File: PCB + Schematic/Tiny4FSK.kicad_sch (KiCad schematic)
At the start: 83 parts, among them J1 Power Ext, J2 GPIO, J3 I2C, J4 USB, J5 USB Breakout, J6 SPI, J7 USBC, J8 SWD, J9 Counterpoise, SW1 Power Switch, SW2 RST, U1 BME280, U2 ATGM336H, U3 TPS61200DRC, U4 ECS-327TXO-2012, U5 ATSAMD21G18A-A, U6 SI4063, U7 Linear Step-Down

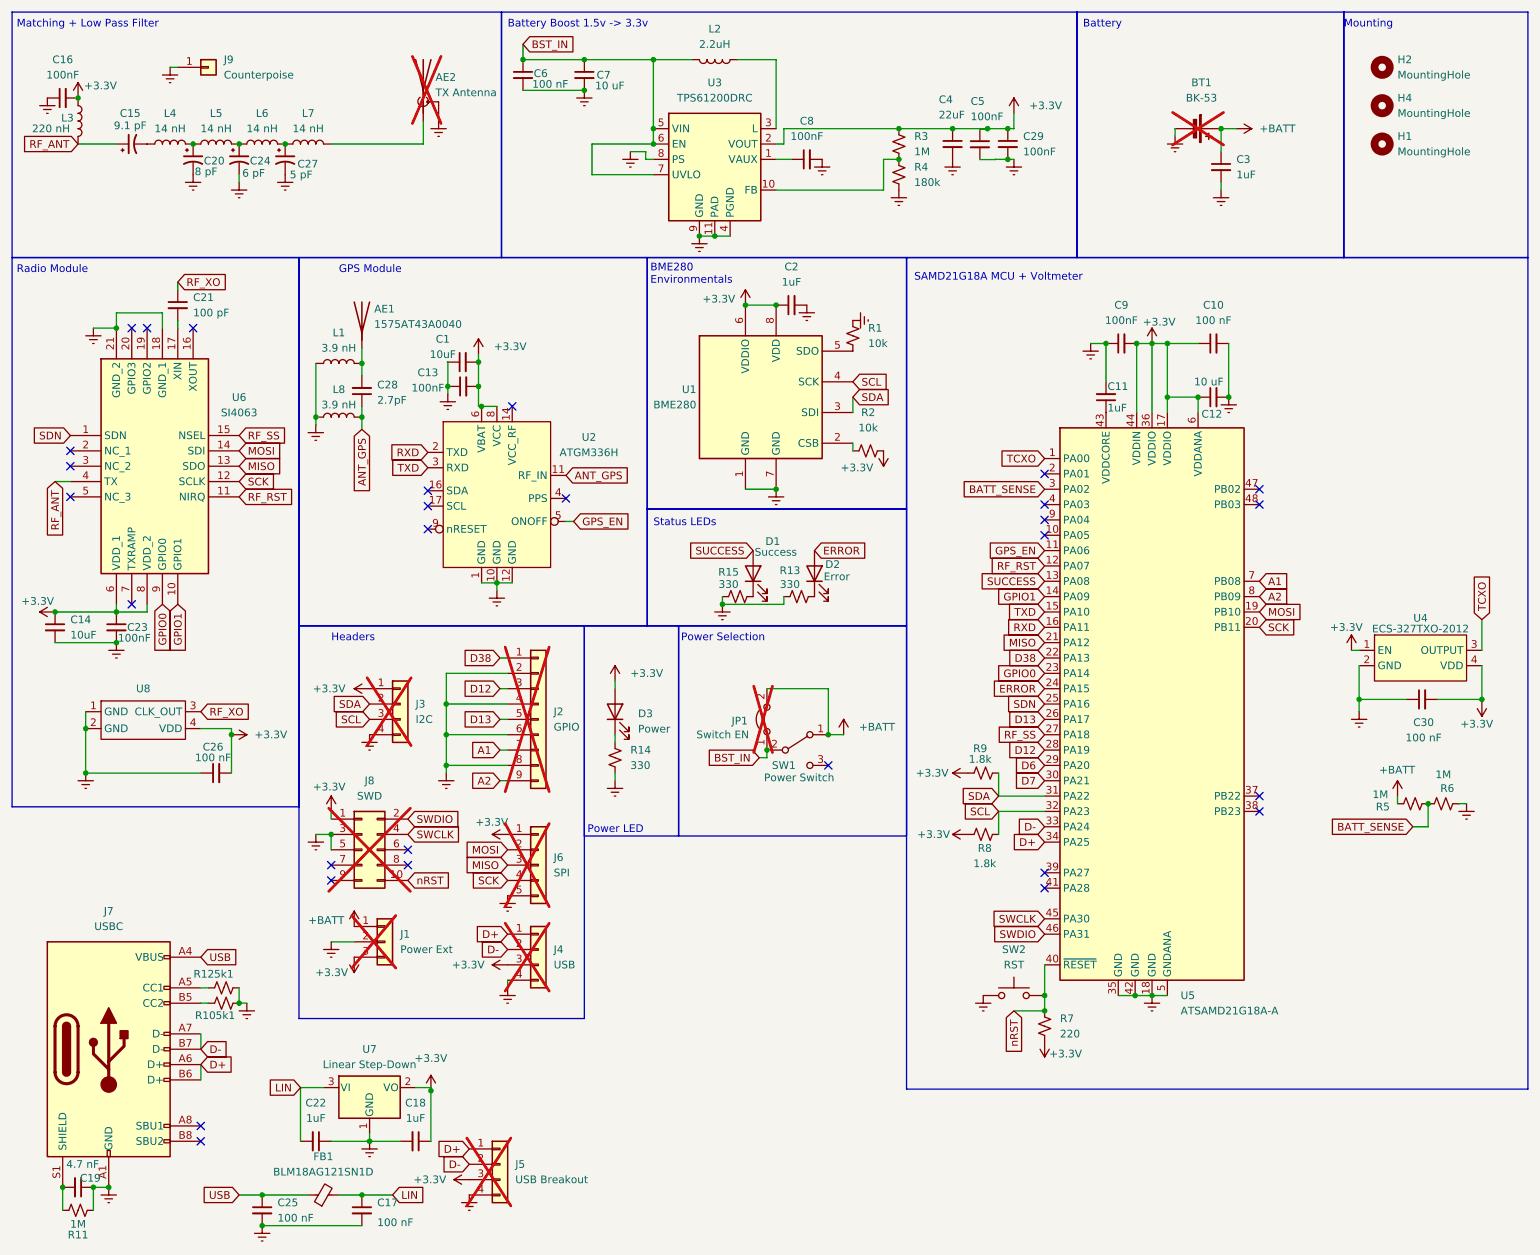
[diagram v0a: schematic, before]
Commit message: split into hierarchical sheets
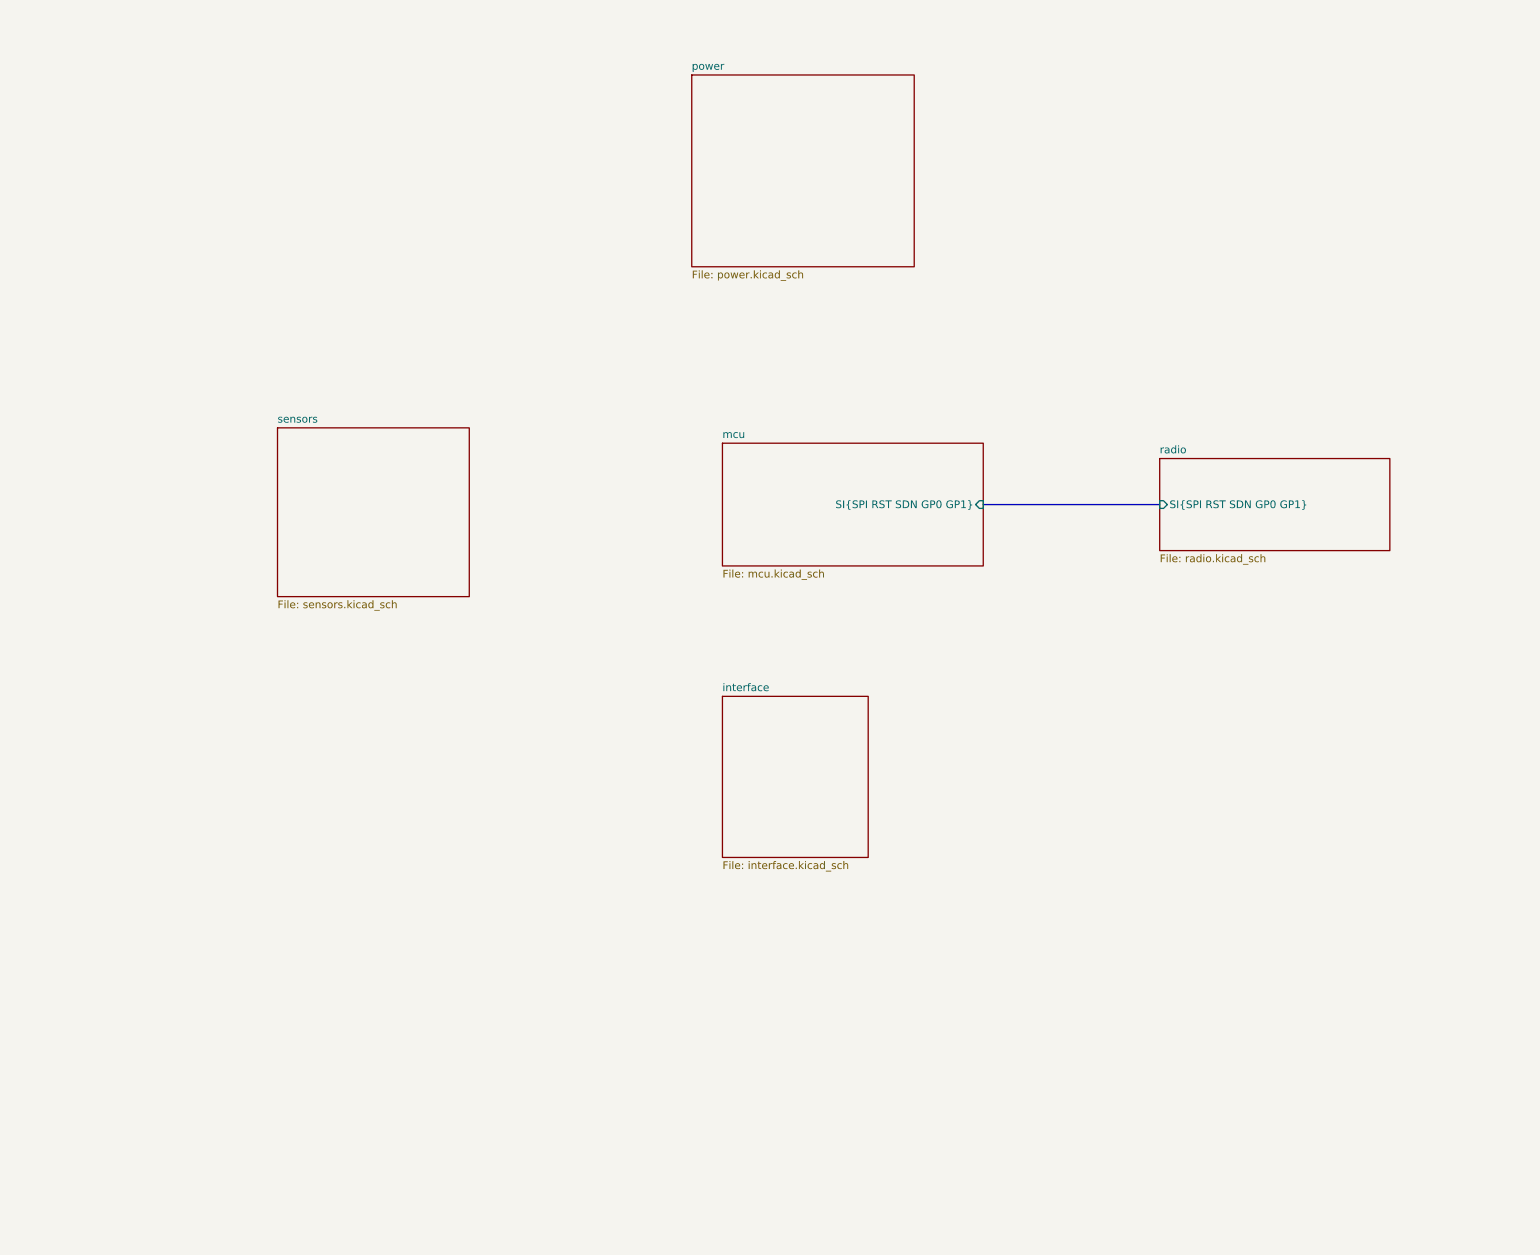
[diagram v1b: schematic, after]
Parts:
- removed AE1: 1575AT43A0040, RF_Antenna_Extended:ANT_1575AT_JOT, symbol Device:Antenna
- removed AE2: TX Antenna, Antenna:Antenna_Whip, symbol Device:Antenna_Shield
- removed BT1: BK-53, BatteryExtended:BAT_53, symbol Device:Battery_Cell
- removed C1, C14: 10uF, Capacitor_SMD:C_0402_1005Metric_Pad0.74x0.62mm_HandSolder, symbol Device:C_Small
- removed C10, C17, C25, C26, C30, C6: 100 nF, Capacitor_SMD:C_0402_1005Metric_Pad0.74x0.62mm_HandSolder, symbol Device:C_Small
- removed C11, C18, C2, C22, C3: 1uF, Capacitor_SMD:C_0402_1005Metric_Pad0.74x0.62mm_HandSolder, symbol Device:C_Small
- removed C12: 10 uF, Capacitor_SMD:C_0402_1005Metric_Pad0.74x0.62mm_HandSolder, symbol Device:C_Small
- removed C13, C16, C23, C29, C5, C8, C9: 100nF, Capacitor_SMD:C_0402_1005Metric_Pad0.74x0.62mm_HandSolder, symbol Device:C_Small
- removed C15: 9.1 pF, Capacitor_SMD:C_0402_1005Metric_Pad0.74x0.62mm_HandSolder, symbol Device:C_Polarized_Small_US
- removed C19: 4.7 nF, Capacitor_SMD:C_0402_1005Metric_Pad0.74x0.62mm_HandSolder, symbol Device:C_Small
- removed C20: 8 pF, Capacitor_SMD:C_0402_1005Metric_Pad0.74x0.62mm_HandSolder, symbol Device:C_Polarized_Small_US
- removed C21: 100 pF, Capacitor_SMD:C_0402_1005Metric_Pad0.74x0.62mm_HandSolder, symbol Device:C_Small
- removed C24: 6 pF, Capacitor_SMD:C_0402_1005Metric_Pad0.74x0.62mm_HandSolder, symbol Device:C_Polarized_Small_US
- removed C27: 5 pF, Capacitor_SMD:C_0402_1005Metric_Pad0.74x0.62mm_HandSolder, symbol Device:C_Polarized_Small_US
- removed C28: 2.7pF, Capacitor_SMD:C_0402_1005Metric_Pad0.74x0.62mm_HandSolder, symbol Device:C_Small
- removed C4: 22uF, Capacitor_SMD:C_0603_1608Metric_Pad1.08x0.95mm_HandSolder, symbol Device:C_Small
- removed C7: 10 uF, Capacitor_SMD:C_0603_1608Metric_Pad1.08x0.95mm_HandSolder, symbol Device:C_Small
- removed D1: Success, LED_SMD:LED_0805_2012Metric_Pad1.15x1.40mm_HandSolder, symbol Device:LED
- removed D2: Error, LED_SMD:LED_0805_2012Metric_Pad1.15x1.40mm_HandSolder, symbol Device:LED
- removed D3: Power, LED_SMD:LED_0805_2012Metric_Pad1.15x1.40mm_HandSolder, symbol Device:LED
- removed FB1: BLM18AG121SN1D, Resistor_SMD:R_0603_1608Metric_Pad0.98x0.95mm_HandSolder, symbol Device:FerriteBead_Small
- removed H1, H2, H4: MountingHole, MountingHole:MountingHole_2.2mm_M2, symbol Mechanical:MountingHole
- removed J1: Power Ext, Connector_PinHeader_2.54mm:PinHeader_1x03_P2.54mm_Vertical, symbol Connector_Generic:Conn_01x03
- removed J2: GPIO, Connector_PinHeader_2.54mm:PinHeader_1x09_P2.54mm_Vertical, symbol Connector_Generic:Conn_01x09
- removed J3: I2C, Connector_PinHeader_2.54mm:PinHeader_1x04_P2.54mm_Vertical, symbol Connector_Generic:Conn_01x04
- removed J4: USB, Connector_PinHeader_2.54mm:PinHeader_1x04_P2.54mm_Vertical, symbol Connector_Generic:Conn_01x04
- removed J5: USB Breakout, Connector_PinHeader_2.54mm:PinHeader_1x04_P2.54mm_Vertical, symbol Connector_Generic:Conn_01x04
- removed J6: SPI, Connector_PinHeader_2.54mm:PinHeader_1x05_P2.54mm_Vertical, symbol Connector_Generic:Conn_01x05
- removed J7: USBC, Connector_USB:USB_C_Receptacle_GCT_USB4105-xx-A_16P_TopMnt_Horizontal, symbol Connector:USB_C_Receptacle_USB2.0
- removed J8: SWD, Connector_PinHeader_1.27mm:PinHeader_2x05_P1.27mm_Vertical_SMD, symbol Connector_Generic:Conn_02x05_Odd_Even
- removed J9: Counterpoise, Connector_PinHeader_2.54mm:PinHeader_1x01_P2.54mm_Vertical, symbol Connector_Generic:Conn_01x01
- removed JP1: Switch EN, Jumper:SolderJumper-2_P1.3mm_Open_Pad1.0x1.5mm, symbol Jumper:Jumper_2_Open
- removed L1, L8: 3.9 nH, Inductor_SMD:L_0402_1005Metric_Pad0.77x0.64mm_HandSolder, symbol Device:L
- removed L2: 2.2uH, IND_CONT:LPS3015222MRB, symbol Device:L
- removed L3: 220 nH, Inductor_SMD:L_0402_1005Metric_Pad0.77x0.64mm_HandSolder, symbol Device:L
- removed L4, L5, L6, L7: 14 nH, Inductor_SMD:L_0402_1005Metric_Pad0.77x0.64mm_HandSolder, symbol Device:L
- removed R1, R2: 10k, Resistor_SMD:R_0402_1005Metric_Pad0.72x0.64mm_HandSolder, symbol Device:R_Small_US
- removed R10, R12: 5k1, Resistor_SMD:R_0402_1005Metric_Pad0.72x0.64mm_HandSolder, symbol Device:R_Small_US
- removed R11, R3, R5, R6: 1M, Resistor_SMD:R_0402_1005Metric_Pad0.72x0.64mm_HandSolder, symbol Device:R_Small_US
- removed R13, R14, R15: 330, Resistor_SMD:R_0402_1005Metric_Pad0.72x0.64mm_HandSolder, symbol Device:R_Small_US
- removed R4: 180k, Resistor_SMD:R_0402_1005Metric_Pad0.72x0.64mm_HandSolder, symbol Device:R_Small_US
- removed R7: 220, Resistor_SMD:R_0402_1005Metric_Pad0.72x0.64mm_HandSolder, symbol Device:R_Small_US
- removed R8, R9: 1.8k, Resistor_SMD:R_0402_1005Metric_Pad0.72x0.64mm_HandSolder, symbol Device:R_Small_US
- removed SW1: Power Switch, Button_Switch_SMD:SW_SPDT_PCM12, symbol Switch:SW_SPDT
- removed SW2: RST, Button_Switch_SMD:SW_Tactile_SPST_NO_Straight_CK_PTS636Sx25SMTRLFS, symbol Switch:SW_Push
- removed U1: BME280, Package_LGA:Bosch_LGA-8_2.5x2.5mm_P0.65mm_ClockwisePinNumbering, symbol Sensor:BME280
- removed U2: ATGM336H, RF_GPS_Extended:ATGM336H, symbol RF_GPS_Extended:ATGM336H
- removed U3: TPS61200DRC, Package_SON:Texas_S-PVSON-N10_ThermalVias, symbol Regulator_Switching:TPS61200DRC
- removed U4: ECS-327TXO-2012, Crystal:Crystal_SMD_3225-4Pin_3.2x2.5mm, symbol Oscillator:ATXK-H11-E-32.768KHZ-E50-T3
- removed U5: ATSAMD21G18A-A, Package_QFP:TQFP-48_7x7mm_P0.5mm, symbol MCU_Microchip_SAMD:ATSAMD21G18A-A
- removed U6: SI4063, Package_DFN_QFN:QFN-20-1EP_4x4mm_P0.5mm_EP2.5x2.5mm_ThermalVias, symbol SI4063:SI4063-C2A-GMR
- removed U7: Linear Step-Down, LDO:MCP1700, symbol Regulator_Linear:MCP1700x-330xxTT
- removed U8: (no value), Oscillator_TCXO:ECS-TXO-20CSMV4, symbol TCXO:20CSMV4
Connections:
- no-connect marks 29 -> 0
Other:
- added sheet interface (interface.kicad_sch)
- added sheet mcu (mcu.kicad_sch)
- added sheet power (power.kicad_sch)
- added sheet radio (radio.kicad_sch)
- added sheet sensors (sensors.kicad_sch)
- note removed: "BME280 Environmentals"
- note removed: "Battery"
- note removed: "Battery Boost 1.5v -> 3.3v"
- note removed: "GPS Module"
- note removed: "Headers"
- note removed: "Matching + Low Pass Filter"
- note removed: "Mounting"
- note removed: "Power LED"
- note removed: "Power Selection"
- note removed: "Radio Module"
- note removed: "SAMD21G18A MCU + Voltmeter"
- note removed: "Status LEDs"

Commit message: add power path and interface busses
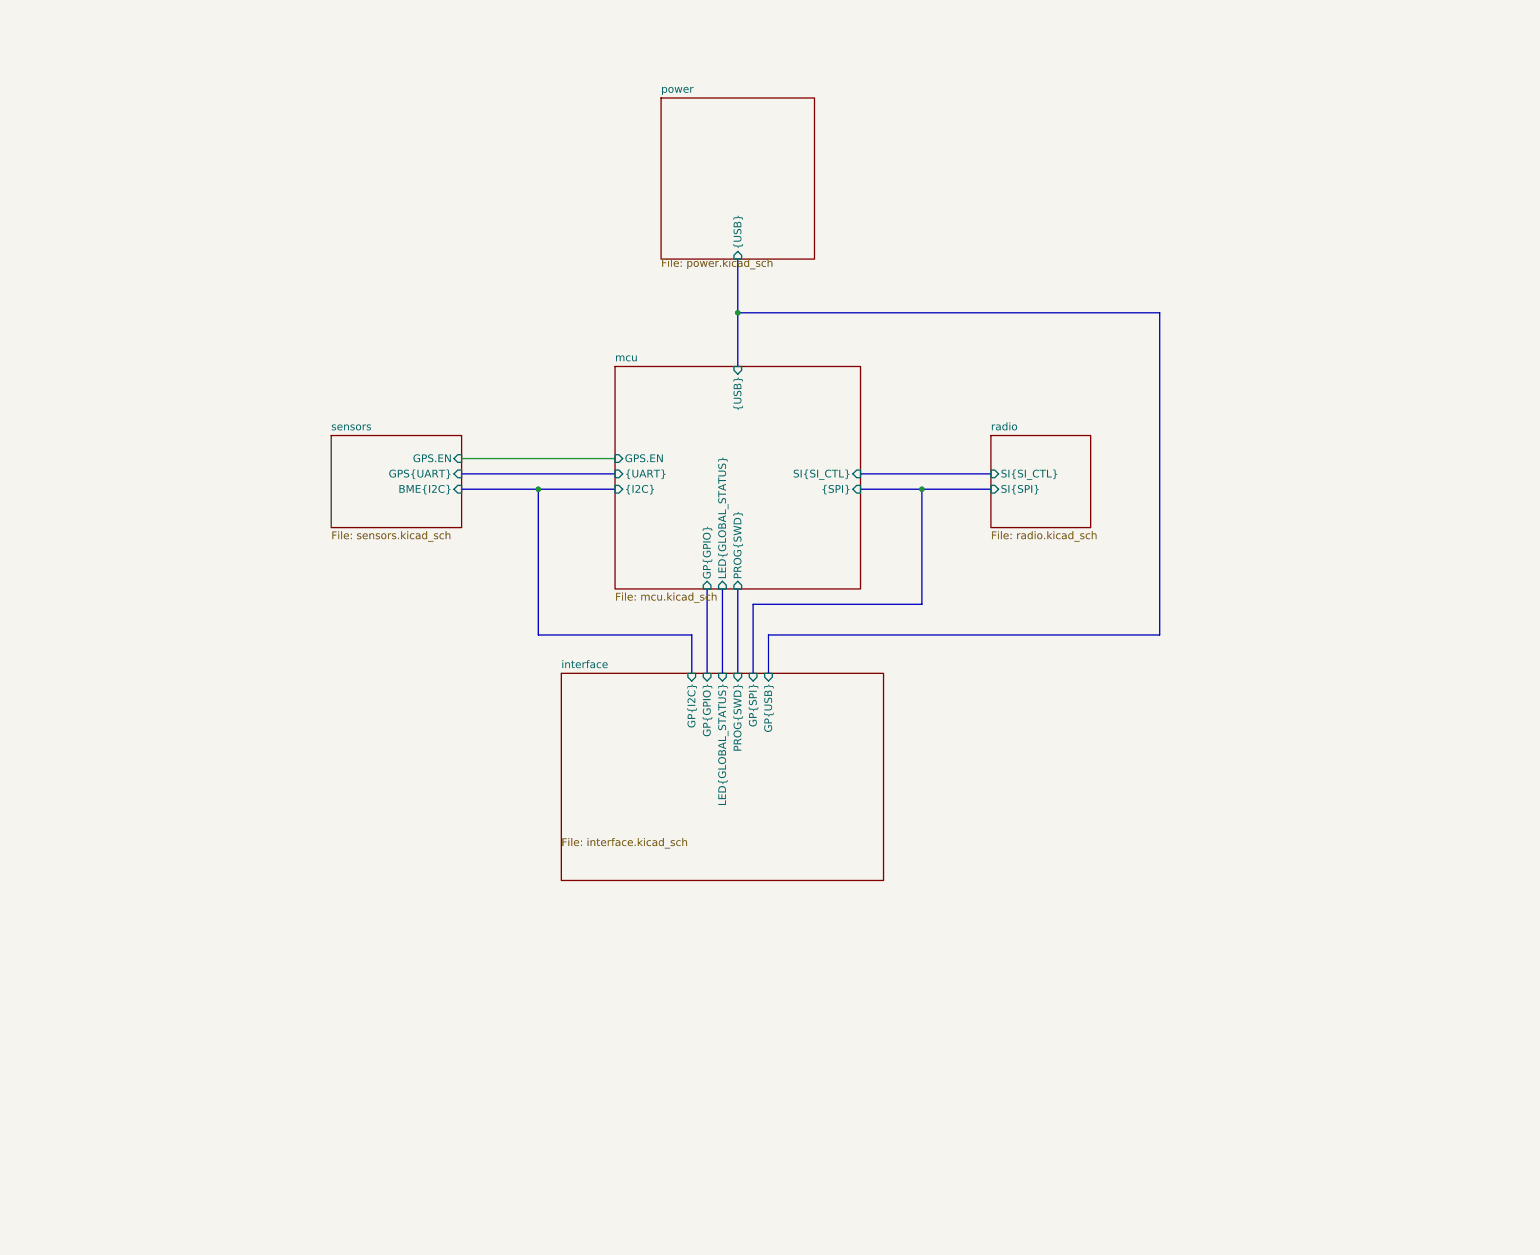
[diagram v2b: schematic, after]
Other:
- sheet interface ports: added GP{GPIO}, GP{I2C}, GP{SPI}, GP{USB}, LED{GLOBAL_STATUS}, PROG{SWD}; removed none
- sheet mcu ports: added GPS.EN, GP{GPIO}, LED{GLOBAL_STATUS}, PROG{SWD}, SI{SI_CTL}, {I2C}, {SPI}, {UART}, {USB}; removed SI{SPI RST SDN GP0 GP1}
- sheet power ports: added {USB}; removed none
- sheet radio ports: added SI{SI_CTL}, SI{SPI}; removed SI{SPI RST SDN GP0 GP1}
- sheet sensors ports: added BME{I2C}, GPS.EN, GPS{UART}; removed none
